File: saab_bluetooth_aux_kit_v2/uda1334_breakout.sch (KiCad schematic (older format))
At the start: 36 parts, among them U1 UDA1334ATS, U2 MIC5225-3.3, X2 19269

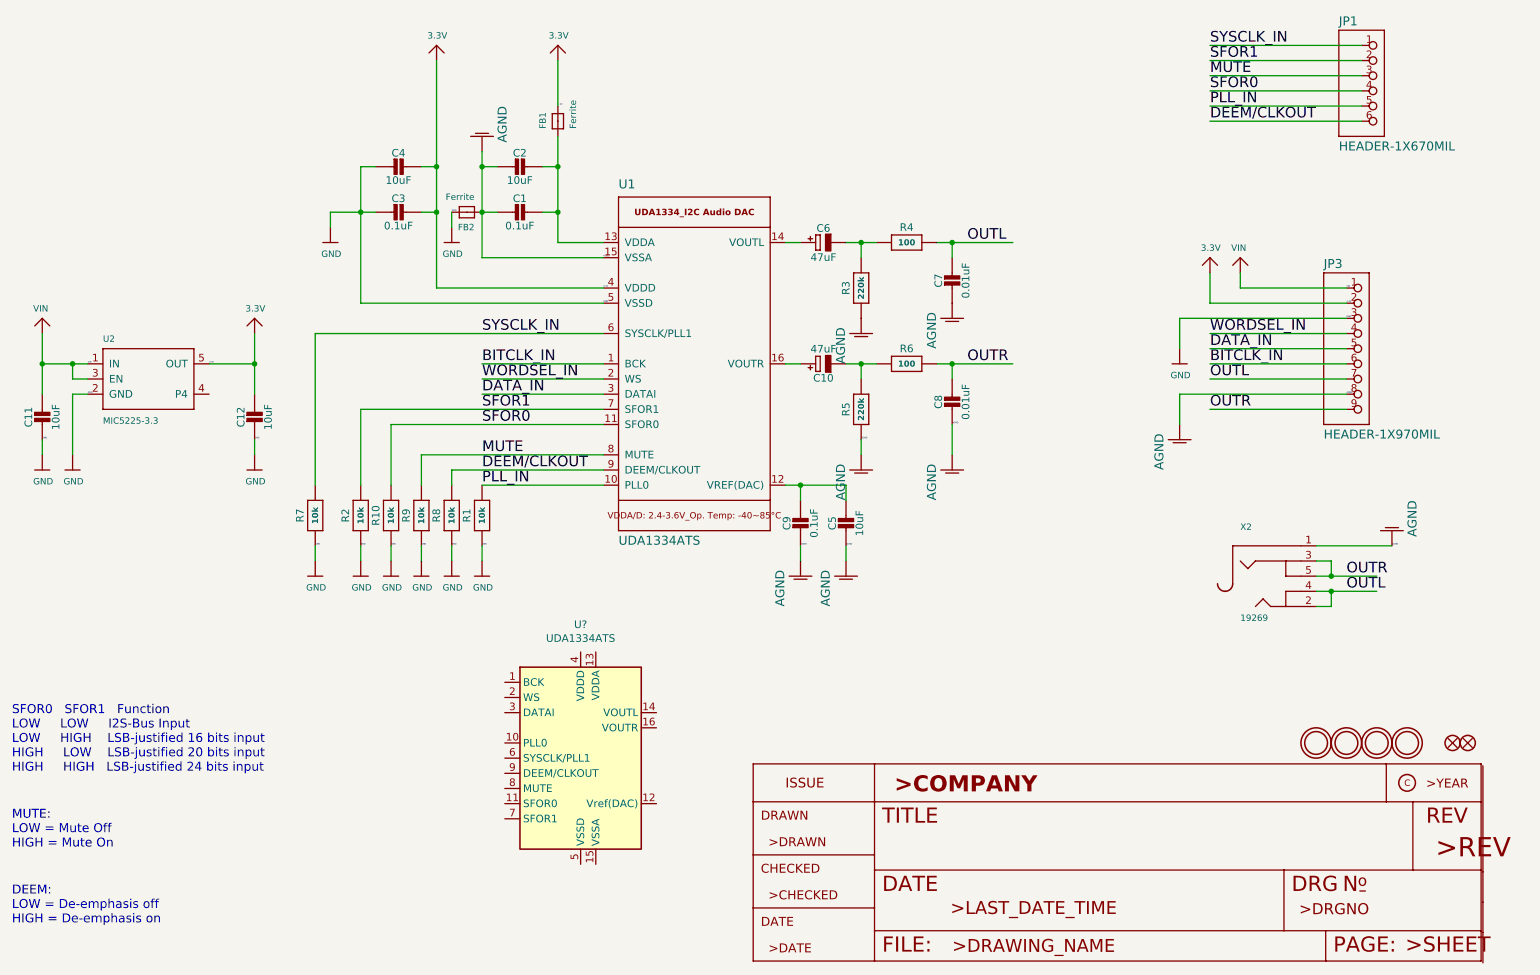
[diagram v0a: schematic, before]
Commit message: Working on new bluetooth+can module from scratch
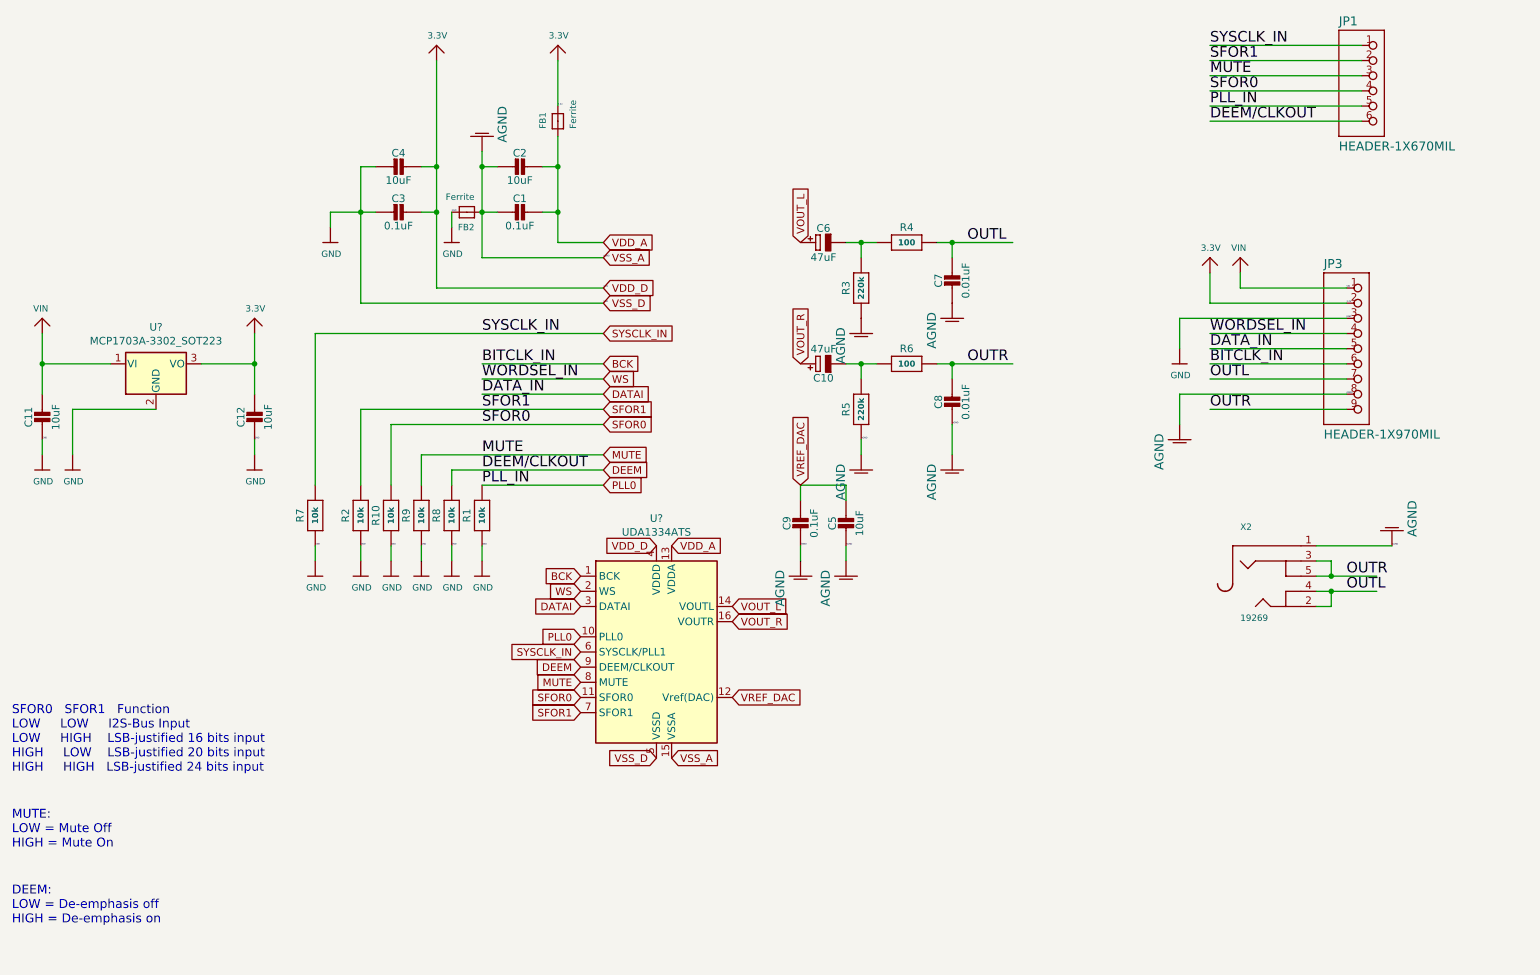
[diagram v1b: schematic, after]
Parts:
- removed FID1, FID2: FIDUCIAL_1MM, saab_bluetooth_aux_kit:FIDUCIAL_1MM, symbol saab_bluetooth_aux_kit-eagle-import:FIDUCIAL_1MM
- removed U$11, U$12, U$13, U$14: MOUNTINGHOLE2.5, saab_bluetooth_aux_kit:MOUNTINGHOLE_2.5_PLATED, symbol saab_bluetooth_aux_kit-eagle-import:MOUNTINGHOLE2.5
- removed U1: UDA1334ATS, saab_bluetooth_aux_kit:SSOP16_4.4MM, symbol saab_bluetooth_aux_kit-eagle-import:AUDIO_I2S_UDA1334""
- removed U2: MIC5225-3.3, saab_bluetooth_aux_kit:SOT23-5, symbol saab_bluetooth_aux_kit-eagle-import:VREG_SOT23-5
- added U?: MCP1703A-3302_SOT223, Package_TO_SOT_SMD:SOT-223-3_TabPin2, symbol Regulator_Linear:MCP1703A-3302_SOT223
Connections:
- net labels added: BCK, DATAI, DEEM, PLL0, VDD_A, VDD_D, VOUT_L, VOUT_R, VREF_DAC, VSS_A, VSS_D, WS
- wire segments 110 -> 104
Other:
- moved on the sheet: U?
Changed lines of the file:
@@
-GND
-Wire Wire Line
-	1800 3400 1700 3400
-Wire Wire Line
-	1700 3400 1700 3800
-Text Label 1800 3400 0    10   ~ 0
 GND
 Wire Wire Line
@@
 OUTR
 Wire Wire Line
-	6400 4000 6500 4000
-Wire Wire Line
 	6500 4000 6500 4100
 Wire Wire Line
@@
 Wire Wire Line
 	6800 4000 6800 4100
-Connection ~ 6500 4000
 Wire Wire Line
 	5200 3900 4200 3900
@@
 3.3V
 Wire Wire Line
-	2600 3200 2900 3200
-Wire Wire Line
 	2900 3200 2900 3000
 Wire Wire Line
 	2900 3400 2900 3200
 Connection ~ 2900 3200
-Text Label 2600 3200 0    10   ~ 0
-3.3V
 Wire Wire Line
 	10100 2800 9200 2800
@@
 3.3V
 Wire Wire Line
-	1800 3200 1700 3200
-Wire Wire Line
-	1700 3200 1500 3200
-Wire Wire Line
 	1500 3200 1500 3000
 Wire Wire Line
-	1800 3300 1700 3300
-Wire Wire Line
-	1700 3300 1700 3200
-Wire Wire Line
 	1500 3400 1500 3200
-Connection ~ 1700 3200
 Connection ~ 1500 3200
-Text Label 1800 3200 0    10   ~ 0
-VIN
 Wire Wire Line
 	10100 2700 9400 2700
@@
 Text Label 10100 2700 0    10   ~ 0
 VIN
-Wire Wire Line
-	6500 3200 6400 3200
-Wire Wire Line
-	6400 2400 6500 2400
 Wire Wire Line
 	5200 2500 4400 2500
@@
 Text Label 10400 4400 0    10   ~ 0
 AGND
-$Comp
-L saab_bluetooth_aux_kit-eagle-import:FRAME_A4 #FRAME1
-U 1 1 73DA64CA
-P 900 7300
-F 0 "#FRAME1" H 900 7300 50  0001 C CNN
-F 1 "FRAME_A4" H 900 7300 50  0001 C CNN
-F 2 "" H 900 7300 50  0001 C CNN
-F 3 "" H 900 7300 50  0001 C CNN
-	1    900  7300
-	1    0    0    -1
-$EndComp
-$Comp
-L saab_bluetooth_aux_kit-eagle-import:FRAME_A4 #FRAME1
-U 2 1 73DA64C6
-P 6200 7200
-F 0 "#FRAME1" H 6200 7200 50  0001 C CNN
-F 1 "FRAME_A4" H 6200 7200 50  0001 C CNN
-F 2 "" H 6200 7200 50  0001 C CNN
-F 3 "" H 6200 7200 50  0001 C CNN
-	2    6200 7200
-	1    0    0    -1
-$EndComp
 $Comp
 L saab_bluetooth_aux_kit-eagle-import:CAP_CERAMIC0805-NOOUTLINE C1
@@
 $EndComp
 $Comp
-L saab_bluetooth_aux_kit-eagle-import:FIDUCIAL_1MM FID1
-U 1 1 DB63CB8D
-P 10900 5700
-F 0 "FID1" H 10900 5700 50  0001 C CNN
-F 1 "FIDUCIAL_1MM" H 10900 5700 50  0001 C CNN
-F 2 "saab_bluetooth_aux_kit:FIDUCIAL_1MM" H 10900 5700 50  0001 C CNN
-F 3 "" H 10900 5700 50  0001 C CNN
-	1    10900 5700
-	1    0    0    -1
-$EndComp
-$Comp
-L saab_bluetooth_aux_kit-eagle-import:FIDUCIAL_1MM FID2
-U 1 1 E067070F
-P 10800 5700
-F 0 "FID2" H 10800 5700 50  0001 C CNN
-F 1 "FIDUCIAL_1MM" H 10800 5700 50  0001 C CNN
-F 2 "saab_bluetooth_aux_kit:FIDUCIAL_1MM" H 10800 5700 50  0001 C CNN
-F 3 "" H 10800 5700 50  0001 C CNN
-	1    10800 5700
-	1    0    0    -1
-$EndComp
-$Comp
-L saab_bluetooth_aux_kit-eagle-import:MOUNTINGHOLE2.5 U$11
-U 1 1 283E49E7
-P 10500 5700
-F 0 "U$11" H 10500 5700 50  0001 C CNN
-F 1 "MOUNTINGHOLE2.5" H 10500 5700 50  0001 C CNN
-F 2 "saab_bluetooth_aux_kit:MOUNTINGHOLE_2.5_PLATED" H 10500 5700 50  0001 C CNN
-F 3 "" H 10500 5700 50  0001 C CNN
-	1    10500 5700
-	1    0    0    -1
-$EndComp
-$Comp
-L saab_bluetooth_aux_kit-eagle-import:MOUNTINGHOLE2.5 U$12
-U 1 1 CB8F9854
-P 10300 5700
-F 0 "U$12" H 10300 5700 50  0001 C CNN
-F 1 "MOUNTINGHOLE2.5" H 10300 5700 50  0001 C CNN
-F 2 "saab_bluetooth_aux_kit:MOUNTINGHOLE_2.5_PLATED" H 10300 5700 50  0001 C CNN
-F 3 "" H 10300 5700 50  0001 C CNN
-	1    10300 5700
-	1    0    0    -1
-$EndComp
-$Comp
-L saab_bluetooth_aux_kit-eagle-import:MOUNTINGHOLE2.5 U$13
-U 1 1 777B985C
-P 10100 5700
-F 0 "U$13" H 10100 5700 50  0001 C CNN
-F 1 "MOUNTINGHOLE2.5" H 10100 5700 50  0001 C CNN
-F 2 "saab_bluetooth_aux_kit:MOUNTINGHOLE_2.5_PLATED" H 10100 5700 50  0001 C CNN
-F 3 "" H 10100 5700 50  0001 C CNN
-	1    10100 5700
-	1    0    0    -1
-$EndComp
-$Comp
-L saab_bluetooth_aux_kit-eagle-import:MOUNTINGHOLE2.5 U$14
-U 1 1 491AF09A
-P 9900 5700
-F 0 "U$14" H 9900 5700 50  0001 C CNN
-F 1 "MOUNTINGHOLE2.5" H 9900 5700 50  0001 C CNN
-F 2 "saab_bluetooth_aux_kit:MOUNTINGHOLE_2.5_PLATED" H 9900 5700 50  0001 C CNN
-F 3 "" H 9900 5700 50  0001 C CNN
-	1    9900 5700
-	1    0    0    -1
-$EndComp
-$Comp
 L saab_bluetooth_aux_kit-eagle-import:GND #U$15
 U 1 1 D0458224
@@
 F 3 "" H 4900 1100 50  0001 C CNN
 	1    4900 1100
-	1    0    0    -1
-$EndComp
-$Comp
-L saab_bluetooth_aux_kit-eagle-import:VREG_SOT23-5 U2
-U 1 1 60D488E9
-P 2200 3300
-F 0 "U2" H 1900 3540 42  0000 L BNN
-F 1 "MIC5225-3.3" H 1900 3000 42  0000 L BNN
-F 2 "saab_bluetooth_aux_kit:SOT23-5" H 2200 3300 50  0001 C CNN
-F 3 "" H 2200 3300 50  0001 C CNN
-	1    2200 3300
 	1    0    0    -1
 $EndComp
@@
 SFOR0   SFOR1   Function\nLOW     LOW     I2S-Bus Input\nLOW     HIGH    LSB-justified 16 bits input \nHIGH     LOW    LSB-justified 20 bits input \nHIGH     HIGH   LSB-justified 24 bits input
 $Comp
-L saab_bluetooth_aux_kit-eagle-import:AUDIO_I2S_UDA1334"" U1
-U 1 1 A34E531C
-P 5800 3200
-F 0 "U1" H 5300 4350 59  0000 L BNN
-F 1 "UDA1334ATS" H 5300 2000 59  0000 L BNN
-F 2 "saab_bluetooth_aux_kit:SSOP16_4.4MM" H 5800 3200 50  0001 C CNN
-F 3 "" H 5800 3200 50  0001 C CNN
-	1    5800 3200
-	1    0    0    -1
-$EndComp
-$Comp
 L Audio:UDA1334ATS U?
 U 1 1 5ED9BB68
-P 5050 5800
-F 0 "U?" H 5050 6681 50  0000 C CNN
-F 1 "UDA1334ATS" H 5050 6590 50  0000 C CNN
-F 2 "Package_SO:SSOP-16_4.4x5.2mm_P0.65mm" H 5050 5800 50  0001 C CNN
-F 3 "http://www.nxp.com/docs/en/data-sheet/UDA1334ATS.pdf" H 5050 5800 50  0001 C CNN
-	1    5050 5800
-	1    0    0    -1
-$EndComp
+P 5550 5100
+F 0 "U?" H 5550 5981 50  0000 C CNN
+F 1 "UDA1334ATS" H 5550 5890 50  0000 C CNN
+F 2 "Package_SO:SSOP-16_4.4x5.2mm_P0.65mm" H 5550 5100 50  0001 C CNN
+F 3 "http://www.nxp.com/docs/en/data-sheet/UDA1334ATS.pdf" H 5550 5100 50  0001 C CNN
+	1    5550 5100
+	1    0    0    -1
+$EndComp
+Text GLabel 6500 4000 1    50   Input ~ 0
+VREF_DAC
+Text GLabel 6500 3200 1    50   Input ~ 0
+VOUT_R
+Text GLabel 6500 2400 1    50   Input ~ 0
+VOUT_L
+Text GLabel 5200 2400 2    50   Input ~ 0
+VDD_A
+Text GLabel 5200 2500 2    50   Input ~ 0
+VSS_A
+Text GLabel 5200 2700 2    50   Input ~ 0
+VDD_D
+Text GLabel 5200 2800 2    50   Input ~ 0
+VSS_D
+Text GLabel 5200 3000 2    50   Input ~ 0
+SYSCLK_IN
+Text GLabel 5200 3200 2    50   Input ~ 0
+BCK
+Text GLabel 5200 3300 2    50   Input ~ 0
+WS
+Text GLabel 5200 3400 2    50   Input ~ 0
+DATAI
+Text GLabel 5200 3500 2    50   Input ~ 0
+SFOR1
+Text GLabel 5200 3600 2    50   Input ~ 0
+SFOR0
+Text GLabel 5200 3800 2    50   Input ~ 0
+MUTE
+Text GLabel 5200 3900 2    50   Input ~ 0
+DEEM
+Text GLabel 5200 4000 2    50   Input ~ 0
+PLL0
+Text GLabel 5050 4600 0    50   Input ~ 0
+BCK
+Text GLabel 5050 4700 0    50   Input ~ 0
+WS
+Text GLabel 5050 4800 0    50   Input ~ 0
+DATAI
+Text GLabel 5050 5000 0    50   Input ~ 0
+PLL0
+Text GLabel 5050 5100 0    50   Input ~ 0
+SYSCLK_IN
+Text GLabel 5050 5200 0    50   Input ~ 0
+DEEM
+Text GLabel 5050 5300 0    50   Input ~ 0
+MUTE
+Text GLabel 5050 5400 0    50   Input ~ 0
+SFOR0
+Text GLabel 5050 5500 0    50   Input ~ 0
+SFOR1
+Text GLabel 6050 5400 2    50   Input ~ 0
+VREF_DAC
+Text GLabel 6050 4900 2    50   Input ~ 0
+VOUT_R
+Text GLabel 6050 4800 2    50   Input ~ 0
+VOUT_L
+Text GLabel 5650 5800 2    50   Input ~ 0
+VSS_A
+Text GLabel 5550 5800 0    50   Input ~ 0
+VSS_D
+Text GLabel 5550 4400 0    50   Input ~ 0
+VDD_D
+Text GLabel 5650 4400 2    50   Input ~ 0
+VDD_A
+$Comp
+L Regulator_Linear:MCP1703A-3302_SOT223 U?
+U 1 1 5EEB1033
+P 2250 3200
+F 0 "U?" H 2250 3442 50  0000 C CNN
+F 1 "MCP1703A-3302_SOT223" H 2250 3351 50  0000 C CNN
+F 2 "Package_TO_SOT_SMD:SOT-223-3_TabPin2" H 2250 3400 50  0001 C CNN
+F 3 "http://ww1.microchip.com/downloads/en/DeviceDoc/20005122B.pdf" H 2250 3150 50  0001 C CNN
+	1    2250 3200
+	1    0    0    -1
+$EndComp
+Wire Wire Line
+	1500 3200 1950 3200
+Wire Wire Line
+	1700 3800 1700 3500
+Wire Wire Line
+	1700 3500 2250 3500
+Wire Wire Line
+	2550 3200 2900 3200
 $EndSCHEMATC
